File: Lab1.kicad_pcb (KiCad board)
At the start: 2 copper layers, 12 parts, among them J1 Conn_02x05_Counter_Clockwise, SW2 CK_KMS2xxG, SW3 CK_KMS2xxG, U1 STM32F407VGTx, Y1 Crystal

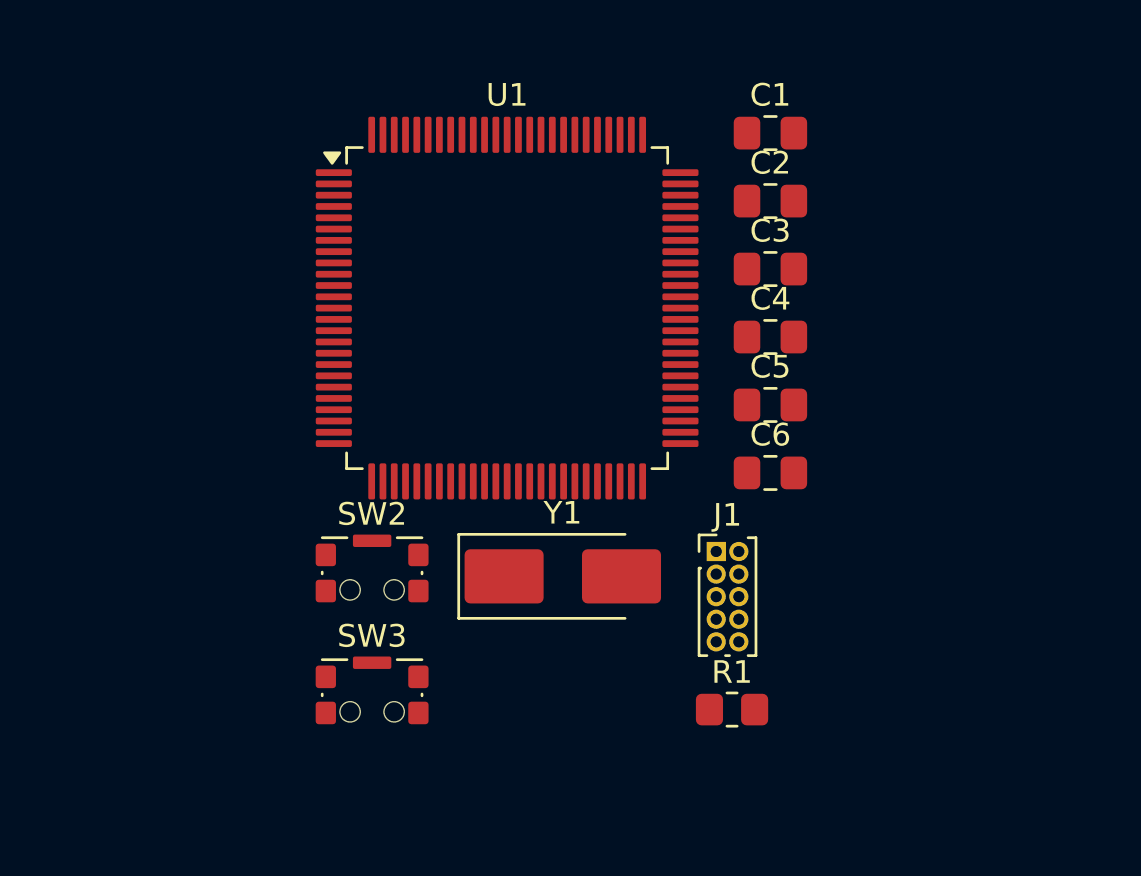
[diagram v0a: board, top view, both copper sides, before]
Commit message: feat: Update footprints for buttons and add Libs
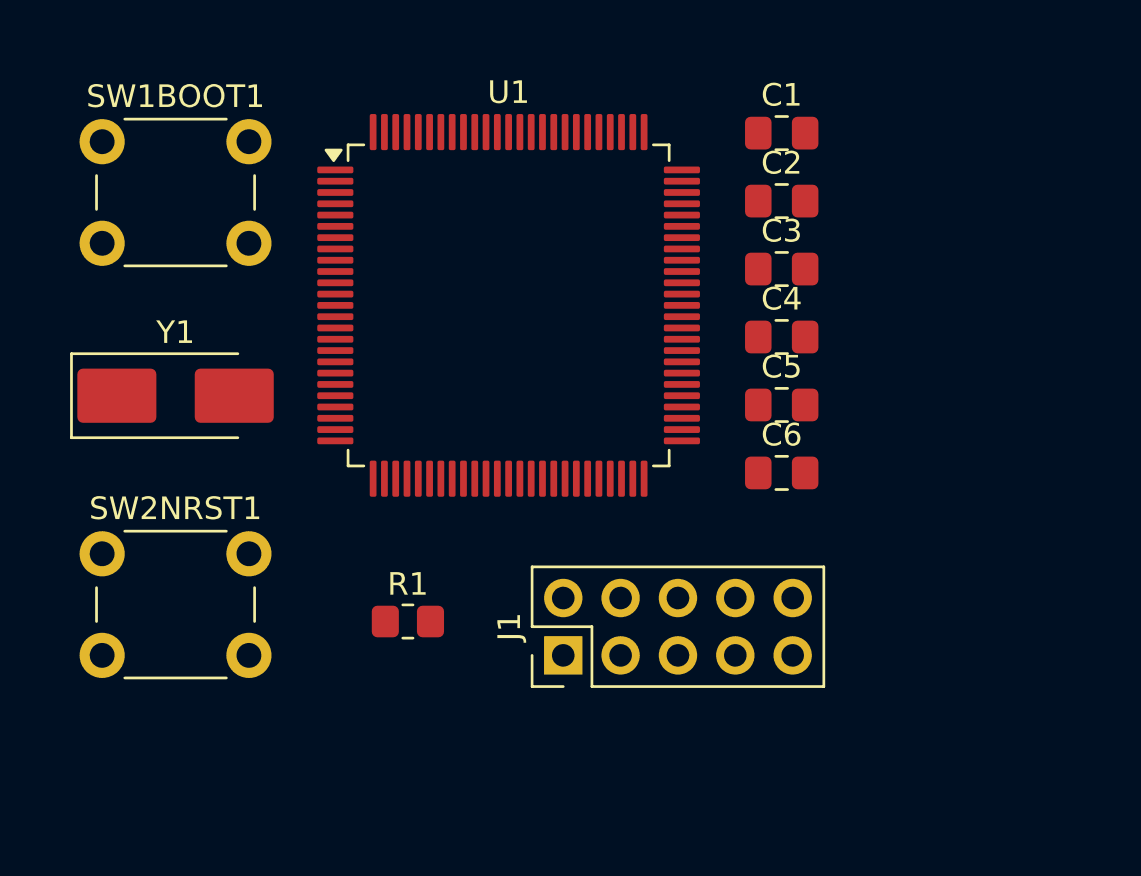
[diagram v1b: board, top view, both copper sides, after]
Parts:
- removed SW2, SW3: CK_KMS2xxG, Button_Switch_SMD:SW_SPST_CK_KMS2xxGP
- added SW1BOOT1: SW_Push, Button_Switch_THT:SW_PUSH_6mm, F.Cu at (120.0, 91.8)
- added SW2NRST1: SW_Push, Button_Switch_THT:SW_PUSH_6mm, F.Cu at (120.0, 110.0)
- J1: footprint Connector_PinHeader_1.00mm:PinHeader_2x05_P1.00mm_Vertical -> Connector_PinHeader_2.54mm:PinHeader_2x05_P2.54mm_Vertical
- moved Y1 18.9 mm to (123.2, 103.0)
- moved R1 14.9 mm to (133.5, 113.0)
- moved J1 8.19 mm to (140.4, 114.5), turned to 90 degrees
- moved C1 0.50 mm to (150.1, 91.4)
- moved C2 0.50 mm to (150.1, 94.4)
- moved C3 0.50 mm to (150.1, 97.4)
- moved C4 0.50 mm to (150.1, 100.4)
- moved C5 0.50 mm to (150.1, 103.4)
- moved C6 0.50 mm to (150.1, 106.4)
- moved U1 0.14 mm to (138.0, 99.0)

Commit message: fix: add ERC power input
feat: structure the diagram into modules

refactor: change global labels to local

feat: add PCB board

feat: make ERC adnd DRC check
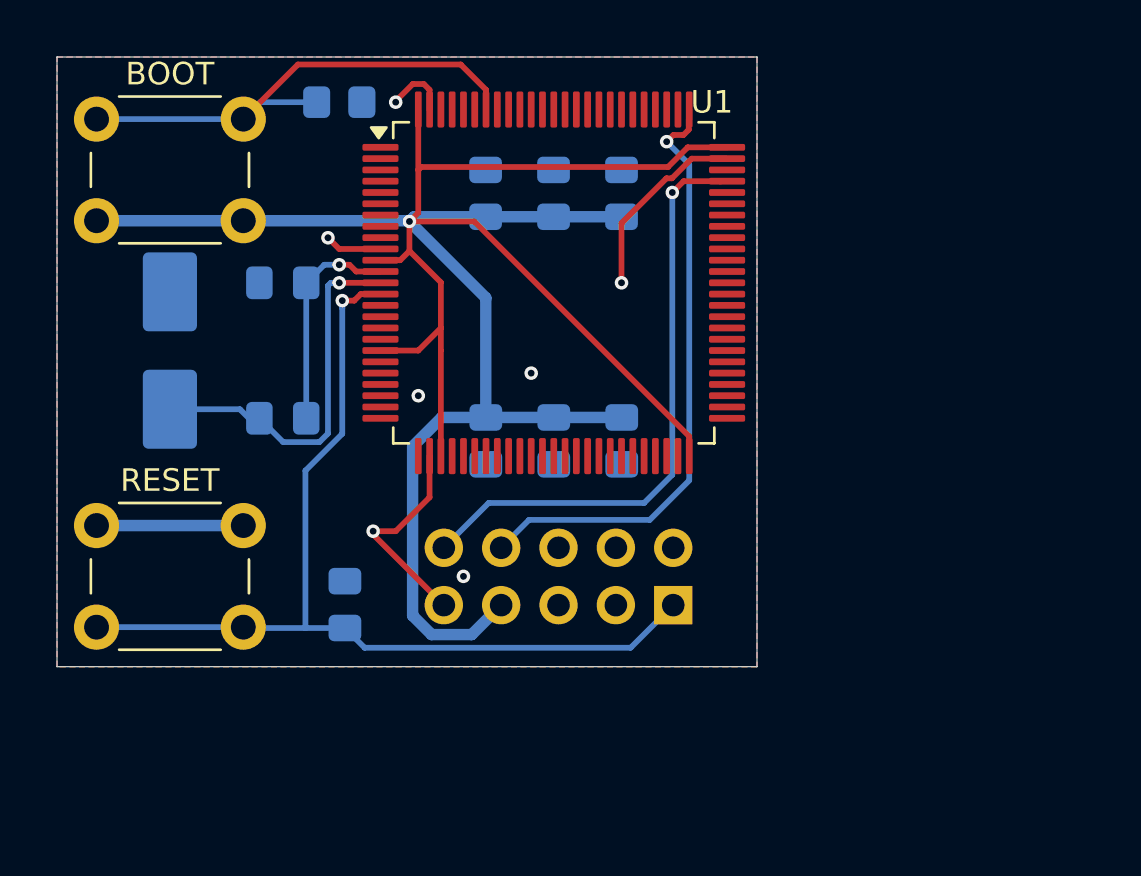
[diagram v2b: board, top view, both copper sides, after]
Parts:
- added C7: C 0.1 μF, Capacitor_SMD:C_0805_2012Metric_Pad1.18x1.45mm_HandSolder, B.Cu at (137.0, 94.0)
- added C8: C 0.1 μF, Capacitor_SMD:C_0805_2012Metric_Pad1.18x1.45mm_HandSolder, B.Cu at (140.0, 94.0)
- added C9: C 0.1 μF, Capacitor_SMD:C_0805_2012Metric_Pad1.18x1.45mm_HandSolder, B.Cu at (143.0, 94.0)
- C1, C2, C3, C4, C5, C6, J1, R1, Y1: moved to B.Cu
- moved R1 23.2 mm to (130.5, 90.0)
- moved C5 22.7 mm to (128.0, 98.0), turned to 180 degrees
- moved C4 22.4 mm to (128.0, 104.0), turned to 180 degrees
- moved C6 20.2 mm to (130.8, 112.2), turned to -90 degrees
- moved C1 18.9 mm to (137.0, 105.0), turned to 90 degrees
- moved C2 14.7 mm to (140.0, 105.0), turned to 90 degrees
- moved C3 10.4 mm to (143.0, 105.0), turned to 90 degrees
- moved J1 5.35 mm to (145.3, 112.3)
- moved U1 2.24 mm to (140.0, 98.0)
- moved Y1 2.02 mm to (123.0, 101.0), turned to -90 degrees
- moved RESET 1.27 mm to (119.8, 108.8)
- moved BOOT 1.03 mm to (119.8, 90.8)
- renumbered SW1BOOT1 to BOOT, SW2NRST1 to RESET
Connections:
- net EXTAL renamed /EXTAL
- net NRST renamed /NRST
- net SWCLK renamed /SWCLK
- net SWDIO renamed /SWDIO
- net XTAL renamed /XTAL
- BOOT pad 2: PWR -> +3.3V
- C1 pad 2: PWR -> +3.3V
- C2 pad 2: PWR -> +3.3V
- C3 pad 2: PWR -> +3.3V
- J1 pad 7: PWR_PROG -> +3.3V
- U1 pad 100: unconnected-(U1-VDD-Pad100) -> +3.3V
- U1 pad 11: unconnected-(U1-VDD-Pad11) -> +3.3V
- U1 pad 19: unconnected-(U1-VDD-Pad19) -> +3.3V
- U1 pad 28: unconnected-(U1-VDD-Pad28) -> +3.3V
- U1 pad 50: unconnected-(U1-VDD-Pad50) -> +3.3V
- U1 pad 6: PWR -> unconnected-(U1-VBAT-Pad6)
- U1 pad 75: unconnected-(U1-VDD-Pad75) -> +3.3V
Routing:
- net +3.3V: track 0.00 -> 107.6 mm, vias 0 -> 1
- net /NRST: track 0.00 -> 44.1 mm, vias 0 -> 1
- net GND: track 0.00 -> 29.9 mm, vias 0 -> 7
- net /SWCLK: track 0.00 -> 27.1 mm, vias 0 -> 1
- net /SWDIO: track 0.00 -> 26.9 mm, vias 0 -> 1
- net Net-(U1-BOOT0): track 0.00 -> 23.1 mm
- net /EXTAL: track 0.00 -> 17.3 mm, vias 0 -> 1
- net /XTAL: track 0.00 -> 10.1 mm, vias 0 -> 1
- added copper zone on B.Cu, net GND
- added copper zone on F.Cu, net GND
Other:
- board outline added: 31 x 27 mm

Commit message: fix: change side J1
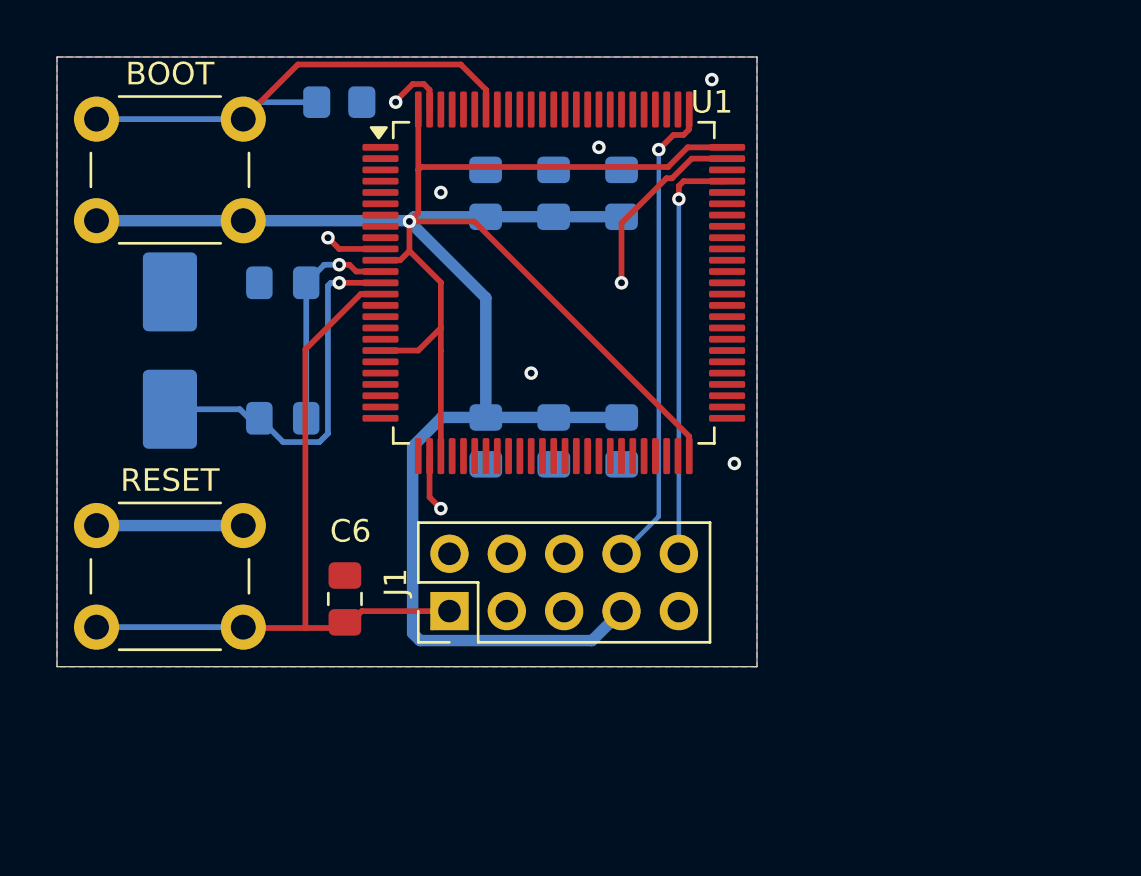
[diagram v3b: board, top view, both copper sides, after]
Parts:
- C6, J1: moved to F.Cu
- moved J1 9.91 mm to (135.4, 112.5)
- moved C6 0.25 mm to (130.8, 112.0)
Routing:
- net /NRST: track 44.1 -> 33.7 mm, vias 1 -> 0
- net /SWDIO: track 26.9 -> 18.8 mm
- net GND: track 29.9 -> 22.9 mm, vias 7 -> 9
- net /SWCLK: track 27.1 -> 21.2 mm
- net +3.3V: track 107.6 -> 113.5 mm

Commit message: feat: add tracing
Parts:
- added D1: LED Blue, LED_SMD:LED_0805_2012Metric, F.Cu at (151.8, 89.8)
- added D2: LED Red, LED_SMD:LED_0805_2012Metric, F.Cu at (155.2, 89.8)
- added D3: LED Orange, LED_SMD:LED_0805_2012Metric, F.Cu at (158.8, 89.8)
- added D4: LED Green, LED_SMD:LED_0805_2012Metric, F.Cu at (162.2, 89.8)
- added R2: R 30 Ohm, Resistor_SMD:R_0805_2012Metric_Pad1.20x1.40mm_HandSolder, F.Cu at (151.8, 94.0)
- added R3: R 100 Ohm, Resistor_SMD:R_0805_2012Metric_Pad1.20x1.40mm_HandSolder, F.Cu at (162.2, 94.0)
- added R4: R 100 Ohm, Resistor_SMD:R_0805_2012Metric_Pad1.20x1.40mm_HandSolder, F.Cu at (158.8, 94.0)
- added R5: R 100 Ohm, Resistor_SMD:R_0805_2012Metric_Pad1.20x1.40mm_HandSolder, F.Cu at (155.2, 94.0)
- added R6: R 10 kOhm, Resistor_SMD:R_0805_2012Metric_Pad1.20x1.40mm_HandSolder, B.Cu at (156.3, 115.5)
- added R7: R 10 kOhm, Resistor_SMD:R_0805_2012Metric_Pad1.20x1.40mm_HandSolder, B.Cu at (156.2, 103.8)
- added RV1: 10 kOhm, Potentiometer_THT:Potentiometer_Bourns_3266Y_Vertical, F.Cu at (135.1, 119.0)
- added RV2: 10 kOhm, Potentiometer_THT:Potentiometer_Bourns_3266Y_Vertical, F.Cu at (146.0, 119.0)
- added User1: SW_Push, Button_Switch_THT:SW_PUSH_6mm, F.Cu at (158.5, 112.0)
- added User2: SW_Push, Button_Switch_THT:SW_PUSH_6mm, F.Cu at (158.5, 100.5)
- renumbered BOOT to SW1BOOT1, RESET to SW2NRST1
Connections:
- U1 pad 15: unconnected-(U1-PC0-Pad15) -> /ADC_1
- U1 pad 16: unconnected-(U1-PC1-Pad16) -> /ADC_2
- U1 pad 57: unconnected-(U1-PD10-Pad57) -> /UButton_1
- U1 pad 58: unconnected-(U1-PD11-Pad58) -> /UButton_2
- U1 pad 59: unconnected-(U1-PD12-Pad59) -> /LED_Green
- U1 pad 60: unconnected-(U1-PD13-Pad60) -> /LED_Orange
- U1 pad 61: unconnected-(U1-PD14-Pad61) -> /LED_Red
- U1 pad 62: unconnected-(U1-PD15-Pad62) -> /LED_Blue
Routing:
- net +3.3V: track 113.5 -> 162.2 mm
- net /ADC_2: track 0.00 -> 29.7 mm, vias 0 -> 1
- net /UButton_1: track 0.00 -> 24.9 mm
- net /ADC_1: track 0.00 -> 22.0 mm, vias 0 -> 1
- net /LED_Green: track 0.00 -> 16.7 mm
- net /UButton_2: track 0.00 -> 16.0 mm
- net /LED_Orange: track 0.00 -> 12.9 mm
- net /LED_Red: track 0.00 -> 9.38 mm
- net /LED_Blue: track 0.00 -> 5.96 mm
- net Net-(D4-K): track 0.00 -> 2.31 mm
- net Net-(D3-K): track 0.00 -> 2.31 mm
- net Net-(D2-K): track 0.00 -> 2.31 mm
- net Net-(D1-K): track 0.00 -> 2.31 mm
- net /NRST: track 33.7 -> 34.3 mm
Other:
- board size 31 x 27 mm -> 46.5 x 34.8 mm
